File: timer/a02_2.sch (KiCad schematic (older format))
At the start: 18 parts, among them U20 74LVC07, U2002 74HC27, U2004 74HC02, U2007 74HC27, U2010 74HC04, U2011 74HC27, U2012 74HC02, U2013 74HC02, U2014 74HC02, U2015 74HC02, U2016 74HC02, U2019 74HC27, U2021 74HC04, U2022 74HC02, U2023 74HC02, U2037 74HC02, U2046 74HC4002

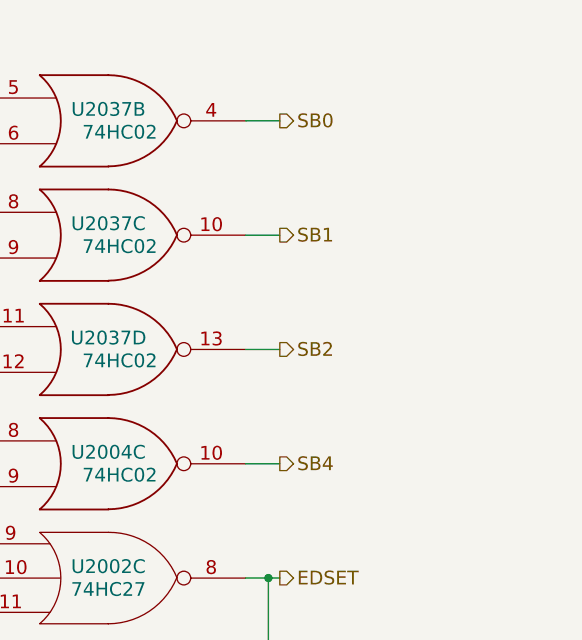
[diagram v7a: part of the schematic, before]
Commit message: Tied in module 7, and corrected lots of errors.
Off the top of my head:
* T12DC/ not actually connected to restart logic in A02-2
* IC12/ and IC13 schematic errors
* Lots of gates moved from later modules up to modules 2-7
* YT0..7 logic dropped from 7, it belongs in 14
* Lots of missing signal breakouts
* ...probably some other things, I should keep a list as I go

All control pulses associated with GOJ1 now behave correctly during
GOJ1.
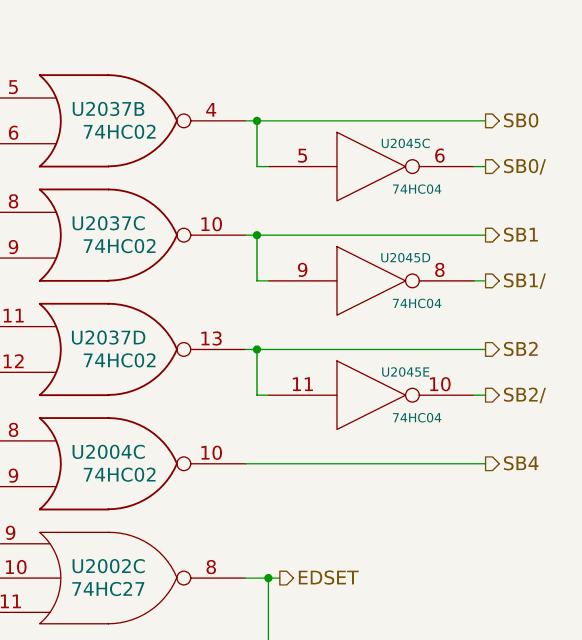
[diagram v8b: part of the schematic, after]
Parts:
- added U2045: 74HC04, symbol 74HC04
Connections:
- net GND: now also U2045.7 (GND), U2045.7 (GND), U2045.7 (GND)
- net SB0: now also U2045.5
- net SB1: now also U2045.9
- net SB2: now also U2045.11
- net VCC: now also U2045.14 (VCC), U2045.14 (VCC), U2045.14 (VCC)
- new net SB0/: U2045.6
- new net SB1/: U2045.8
- new net SB2/: U2045.10
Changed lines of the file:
@@
 	9950 4450 9950 4400
 $Comp
-L VCC #PWR05
+L VCC #PWR04
 U 1 1 56247B70
 P 9950 4400
-F 0 "#PWR05" H 9950 4250 50  0001 C CNN
+F 0 "#PWR04" H 9950 4250 50  0001 C CNN
 F 1 "VCC" H 9950 4550 50  0000 C CNN
 F 2 "" H 9950 4400 60  0000 C CNN
@@
 Text Label 16050 1150 0    60   ~ 0
 P05
-Text HLabel 17650 1050 2    60   Output ~ 0
+Text HLabel 18550 1050 2    60   Output ~ 0
 SB0
 Wire Wire Line
-	17650 1050 17500 1050
+	18550 1050 17500 1050
 $Comp
 L 74HC02 U2037
@@
 $EndComp
 Wire Wire Line
-	17500 1550 17650 1550
-Text HLabel 17650 1550 2    60   Output ~ 0
+	17500 1550 18550 1550
+Text HLabel 18550 1550 2    60   Output ~ 0
 SB1
-Text HLabel 17650 2050 2    60   Output ~ 0
+Text HLabel 18550 2050 2    60   Output ~ 0
 SB2
 Wire Wire Line
-	17650 2050 17500 2050
-Text HLabel 17650 2550 2    60   Output ~ 0
+	17500 2050 18550 2050
+Text HLabel 18550 2550 2    60   Output ~ 0
 SB4
 Wire Wire Line
-	17650 2550 17500 2550
+	18550 2550 17500 2550
 Wire Wire Line
 	16300 1450 16050 1450
@@
 Text HLabel 12950 7650 2    60   Output ~ 0
 TIMR
+$Comp
+L 74HC04 U2045
+U 3 1 56879AB5
+P 18050 1250
+F 0 "U2045" H 18200 1350 40  0000 C CNN
+F 1 "74HC04" H 18250 1150 40  0000 C CNN
+F 2 "" H 18050 1250 60  0000 C CNN
+F 3 "" H 18050 1250 60  0000 C CNN
+	3    18050 1250
+	1    0    0    -1
+$EndComp
+$Comp
+L 74HC04 U2045
+U 4 1 56879C44
+P 18050 1750
+F 0 "U2045" H 18200 1850 40  0000 C CNN
+F 1 "74HC04" H 18250 1650 40  0000 C CNN
+F 2 "" H 18050 1750 60  0000 C CNN
+F 3 "" H 18050 1750 60  0000 C CNN
+	4    18050 1750
+	1    0    0    -1
+$EndComp
+$Comp
+L 74HC04 U2045
+U 5 1 56879E0E
+P 18050 2250
+F 0 "U2045" H 18200 2350 40  0000 C CNN
+F 1 "74HC04" H 18250 2150 40  0000 C CNN
+F 2 "" H 18050 2250 60  0000 C CNN
+F 3 "" H 18050 2250 60  0000 C CNN
+	5    18050 2250
+	1    0    0    -1
+$EndComp
+Wire Wire Line
+	17550 2050 17550 2250
+Wire Wire Line
+	17550 2250 17600 2250
+Connection ~ 17550 2050
+Wire Wire Line
+	18500 2250 18550 2250
+Text HLabel 18550 2250 2    60   Output ~ 0
+SB2/
+Wire Wire Line
+	18500 1750 18550 1750
+Text HLabel 18550 1750 2    60   Output ~ 0
+SB1/
+Wire Wire Line
+	17600 1750 17550 1750
+Wire Wire Line
+	17550 1750 17550 1550
+Connection ~ 17550 1550
+Wire Wire Line
+	18500 1250 18550 1250
+Text HLabel 18550 1250 2    60   Output ~ 0
+SB0/
+Wire Wire Line
+	17600 1250 17550 1250
+Wire Wire Line
+	17550 1250 17550 1050
+Connection ~ 17550 1050
 $EndSCHEMATC
